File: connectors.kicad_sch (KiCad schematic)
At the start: 30 parts, among them J7002 PinHeader_1x3_P2.54mm_SMD, J7003 Tag-Connect_TC2050-IDC-NL_2x5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, J7004 USB-C_GCT_USB4105-GF-A, U7001 FT232RL, U7002 FT2232HL-REEL

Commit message: [#103753] Fix issues according to the review, add FT2232 to the schematic
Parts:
- removed C7002: C_1u_0603, antmicro-footprints:C_0603_1608Metric, symbol Antmicro Symbols:C_1u_0603
- removed C7003, C7004, C7005: C_100n_0402, antmicro-footprints:C_0402_1005Metric, symbol Capacitors0402:C_100n_0402
- removed J7002: PinHeader_1x3_P2.54mm_SMD, antmicro-footprints:PinHeader_1x3_P2.54mm_SMD, symbol Antmicro Symbols:PinHeader_1x3_P2.54mm_SMD
- removed R7008: R_10k_0402, antmicro-footprints:R_0402_1005Metric, symbol Antmicro Symbols:R_10k_0402
- removed U7001: FT232RL, Package_SO:SSOP-28_5.3x10.2mm_P0.65mm, symbol Interface_USB:FT232RL
- added C7014, C7015: C_30p_0402, antmicro-footprints:C_0402_1005Metric, symbol Antmicro Symbols:C_30p_0402
- added C7016, C7017, C7018, C7020, C7021: C_100n_16V_X7R_0402, antmicro-footprints:C_0402_1005Metric, symbol Antmicro Symbols:C_100n_16V_X7R_0402
- added C7019: C_4u7_10V_X7T_0402, antmicro-footprints:C_0402_1005Metric, symbol Capacitors0402:C_4u7_10V_X7T_0402
- added R7008, R7014, R7015, R7016: R_0R_0402, antmicro-footprints:R_0402_1005Metric, symbol Antmicro Symbols:R_0R_0402
- added R7012: R_15k_0402, antmicro-footprints:R_0402_1005Metric, symbol Antmicro Symbols:R_15k_0402
- added R7013: R_10k_0402, antmicro-footprints:R_0402_1005Metric, symbol Antmicro Symbols:R_10k_0402
- added Y7001: Resonator_12MHz_KX-7, antmicro-footprints:Resonator_SMD_Geyer_KX-7_3.2x2.5x0.8mm, symbol Antmicro Symbols:Resonator_12MHz_KX-7
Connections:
- net GNDREF is gone; now on net GND: J7004.SH
- net +3V3: now also U7002.12 (VCORE), U7002.37 (VCORE), U7002.64 (VCORE), C7016.2, C7017.2, C7018.2
- net EC_UART0.RX: now also R7014.2
- net EC_UART0.TX: now also R7008.2
- net EC_UART1.RX: now also R7016.2
- net EC_UART1.TX: now also R7015.2
- net GND: now also U7002.13 (TEST), C7014.1, C7015.1, C7016.1, C7017.1, C7018.1, C7019.1, C7020.1, C7021.1, R7013.1, Y7001.2 (SH), Y7001.4 (SH)
- net USB_R_D+: now reaches D7001.1, J7004.A6 (D_{A}+), J7004.B6 (D_{B}+), R7010.1
- net USB_R_D-: now reaches D7001.2, J7004.A7 (D_{A}-), J7004.B7 (D_{B}-), R7011.1
- net ~{RESET}: now reaches U7002.14 (~{RESET})
- net ~{RESET}: now also R7012.1, R7013.2
- net at U7002.16 (ADBUS0): now also R7008.1
- net at U7002.17 (ADBUS1): now also R7014.1
- net at U7002.2 (OSCI): now also C7015.2, Y7001.1
- net at U7002.3 (OSCO): now also C7014.2, Y7001.3
- net ~{SUSPEND}: now reaches U7002.36 (~{SUSPEND})
- net at U7002.38 (BDBUS0): now also R7015.1
- net at U7002.39 (BDBUS1): now also R7016.1
- net VCC: now reaches U7002.49 (VREGOUT)
- net VCC: now also U7002.50 (VREGIN), C7019.2, C7020.2, C7021.2
- net ~{PWREN}: now reaches U7002.60 (~{PWREN})
- net USB_D-: now reaches R7011.2, U7002.7 (DM)
- net USB_D+: now reaches R7010.2, U7002.8 (DP)
- net at J7004.A4 (VBUS), J7004.A9 (VBUS), J7004.B4 (VBUS)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: now also R7012.2
- no-connect marks 19 -> 5
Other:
- note added: "Internal LDO 1V8"
- note removed: "UART"
- moved on the sheet: C7001, C7006, C7007, C7008, C7009, C7010, C7011, C7012, C7013, D7001, J7003, J7004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

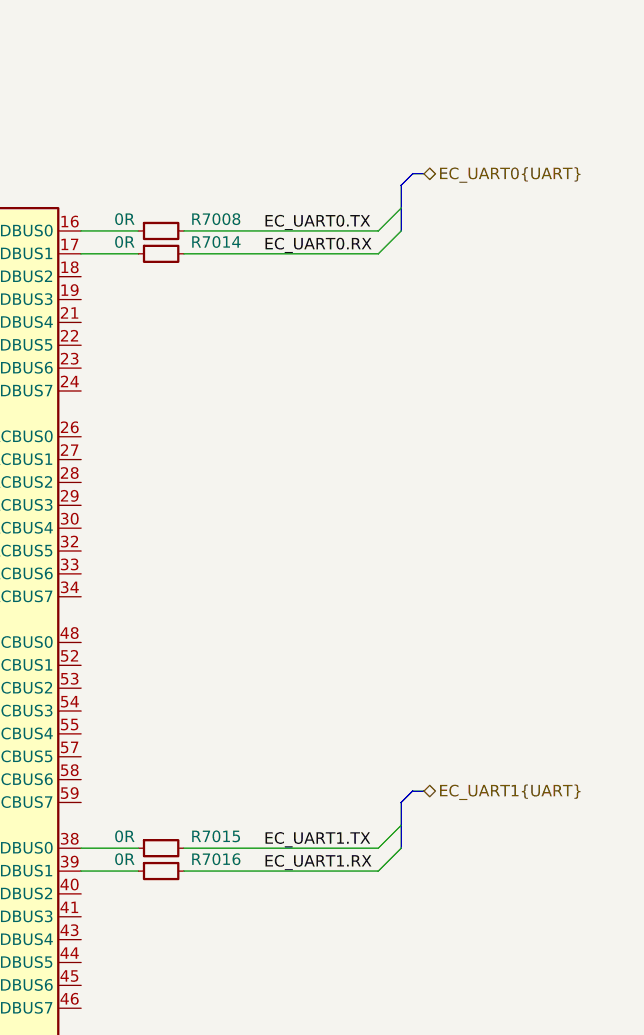
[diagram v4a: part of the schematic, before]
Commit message: [#103753] Fix issues according to the review, add redundant LEDs, delete fp-lib-table
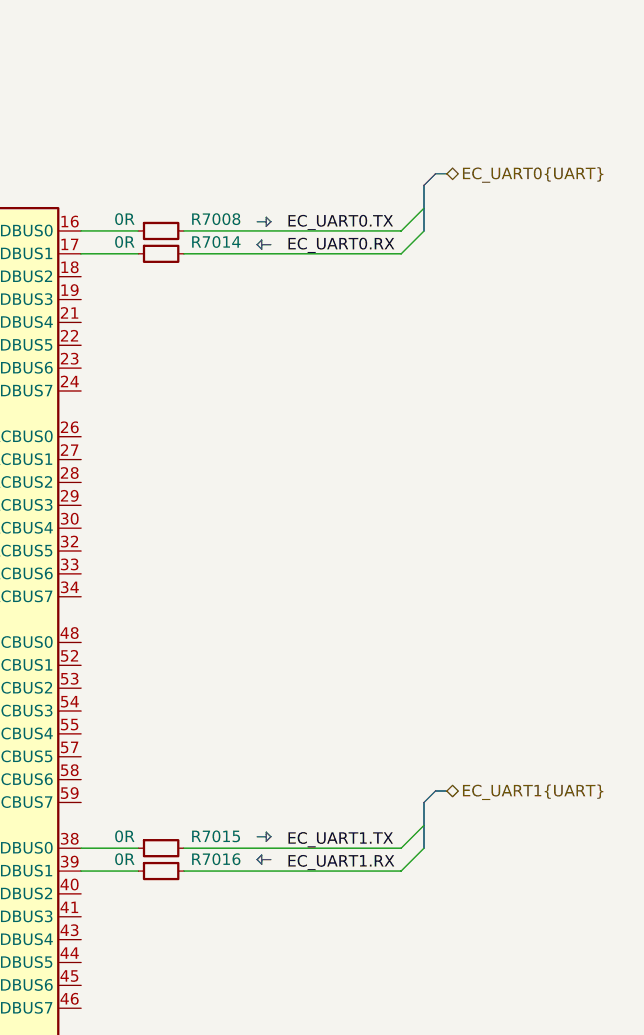
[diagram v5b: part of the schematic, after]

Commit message: [#103753] Update symbol libraries
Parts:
- C7001: symbol Antmicro Symbols:C_1u_0402 -> antmicroCapacitors0402:C_1u_0402
- C7006, C7007, C7019: symbol Capacitors0402:C_4u7_10V_X7T_0402 -> antmicroCapacitors0402:C_4u7_10V_X7T_0402
- C7008, C7009, C7010, C7011, C7012, C7013, C7016, C7017, C7018, C7020, C7021: symbol Antmicro Symbols:C_100n_16V_X7R_0402 -> antmicroCapacitors0402:C_100n_16V_X7R_0402
- C7014, C7015: symbol Antmicro Symbols:C_30p_0402 -> antmicroCapacitors0402:C_30p_0402
- J7003: symbol Antmicro Symbols:Tag-Connect_TC2050-IDC-NL_2x5_P1.27mm -> antmicroTestPoints:Tag-Connect_TC2050-IDC-NL_2x5_P1.27mm
- R7001, R7002, R7003, R7004, R7013: symbol Antmicro Symbols:R_10k_0402 -> antmicroResistors0402:R_10k_0402
- R7005: symbol Antmicro Symbols:R_100k_0402 -> antmicroResistors0402:R_100k_0402
- R7008, R7014, R7015, R7016: symbol Antmicro Symbols:R_0R_0402 -> antmicroResistors0402:R_0R_0402
- R7009: symbol Antmicro Symbols:R_12k_0402 -> antmicroResistors0402:R_12k_0402
- R7012: symbol Antmicro Symbols:R_15k_0402 -> antmicroResistors0402:R_15k_0402
- U7002: symbol Antmicro Symbols:FT2232HL-REEL -> antmicroInterfaceControllers:FT2232HL-REEL
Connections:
- no-connect marks 5 -> 33
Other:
- note removed: "Internal LDO 1V8"

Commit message: [#103753] Fixed issues according to the review
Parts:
- removed C7014, C7015: C_30p_0402, antmicro-footprints:C_0402_1005Metric, symbol antmicroCapacitors0402:C_30p_0402
- removed R7010, R7011: R_10R_0402, antmicro-footprints:R_0402_1005Metric, symbol Antmicro Symbols:R_10R_0402
- added C7002, C7003: C_18p_0402, antmicro-footprints:C_0402_1005Metric, symbol antmicroCapacitors0402:C_18p_0402
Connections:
- net USB_R_D+ is gone; now on net USB_D+: D7001.1, J7004.A6 (D_{A}+), J7004.B6 (D_{B}+)
- net USB_R_D- is gone; now on net USB_D-: D7001.2, J7004.A7 (D_{A}-), J7004.B7 (D_{B}-)
- net +3V3: now also C7021.2, U7002.50 (VREGIN); no longer C7016.2, C7017.2, C7018.2, U7002.12 (VCORE), U7002.37 (VCORE), U7002.64 (VCORE)
- net GND: now also R7012.1, C7002.1, C7003.1; no longer R7013.1
- net VCC: now also C7016.2, C7017.2, C7018.2, U7002.12 (VCORE), U7002.37 (VCORE), U7002.64 (VCORE); no longer C7021.2, U7002.50 (VREGIN)
- net ~{RESET}: now also R7012.2, R7013.1; no longer R7012.1, R7013.2
- net at J7004.A4 (VBUS), J7004.A9 (VBUS), J7004.B4 (VBUS)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: now also R7013.2; no longer R7012.2
- net at U7002.2 (OSCI), Y7001.1: now also C7003.2
- net at U7002.3 (OSCO), Y7001.3: now also C7002.2
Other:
- note added: "VCC - 1V8 from internal LDO"
